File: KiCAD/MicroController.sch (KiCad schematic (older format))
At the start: 0 parts

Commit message: completed 5V buck schematic and setup
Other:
- note added: "atmega and supp"
- note added: "icsp and reset"
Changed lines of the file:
@@
 LIBS:contrib
 LIBS:valves
+LIBS:TPS565208
 LIBS:OBC-PDB-cache
 EELAYER 25 0
@@
 $Descr A4 11693 8268
 encoding utf-8
-Sheet 1 6
+Sheet 3 6
 Title ""
 Date ""
@@
 Comment4 ""
 $EndDescr
+Text Notes 3650 2250 0    118  ~ 0
+atmega and supp
+Text Notes 8400 1950 0    118  ~ 0
+icsp and reset
 $EndSCHEMATC

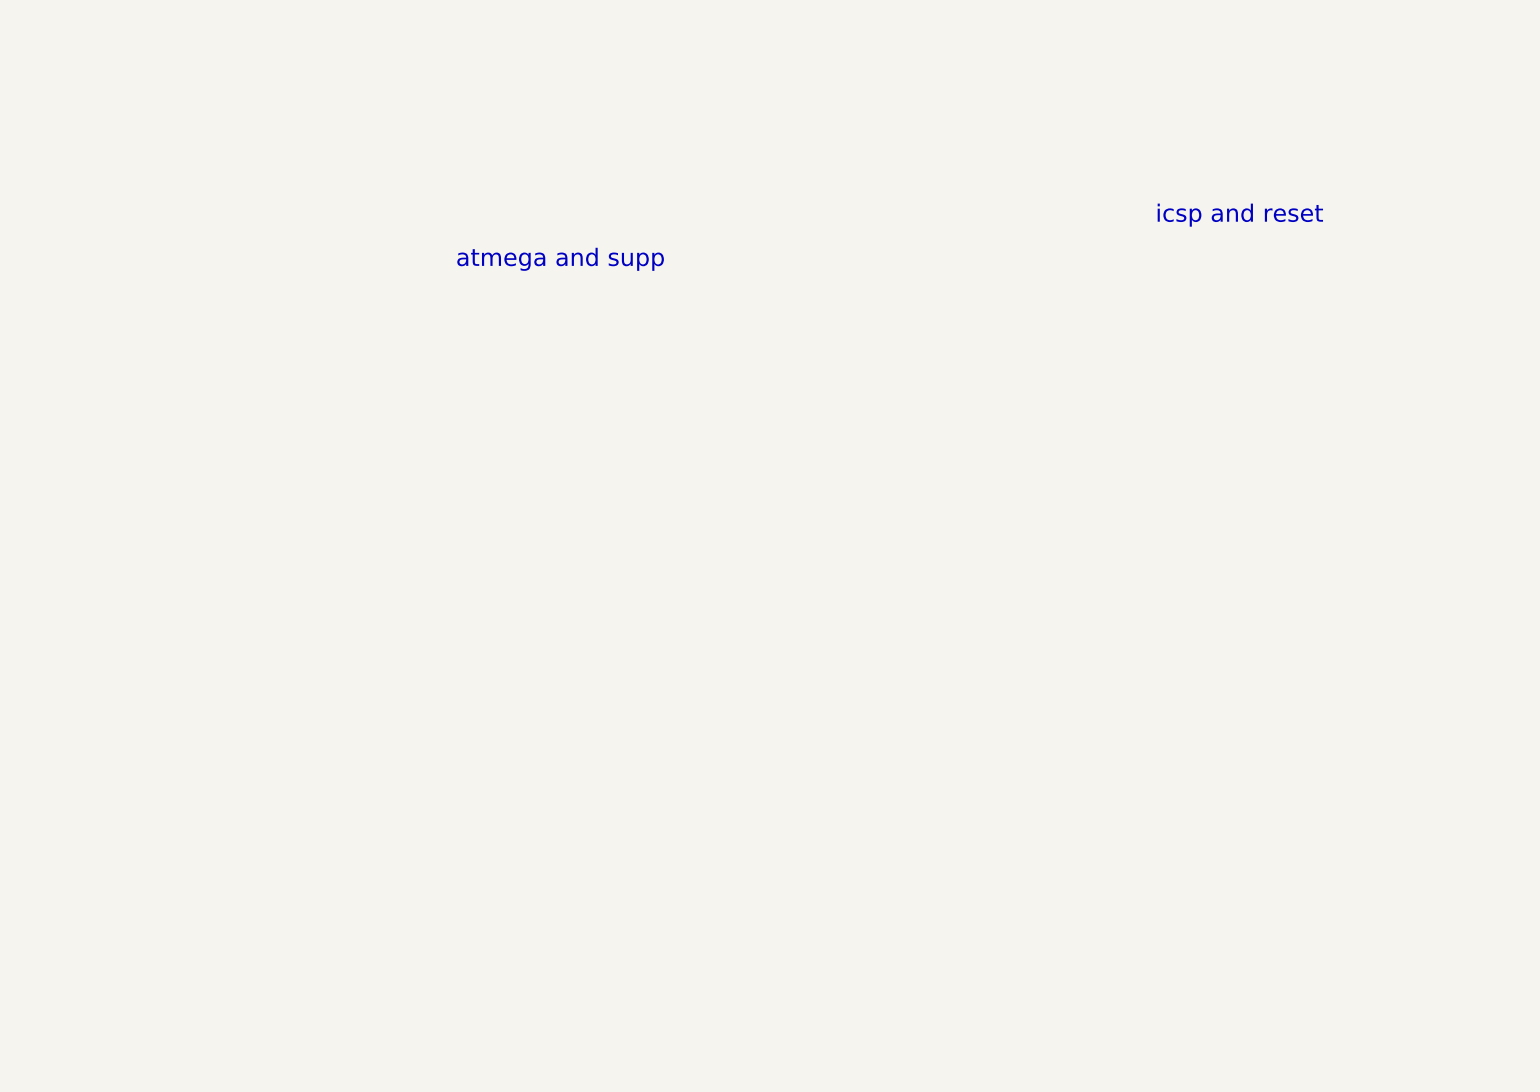
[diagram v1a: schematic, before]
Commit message: added MC but N/C
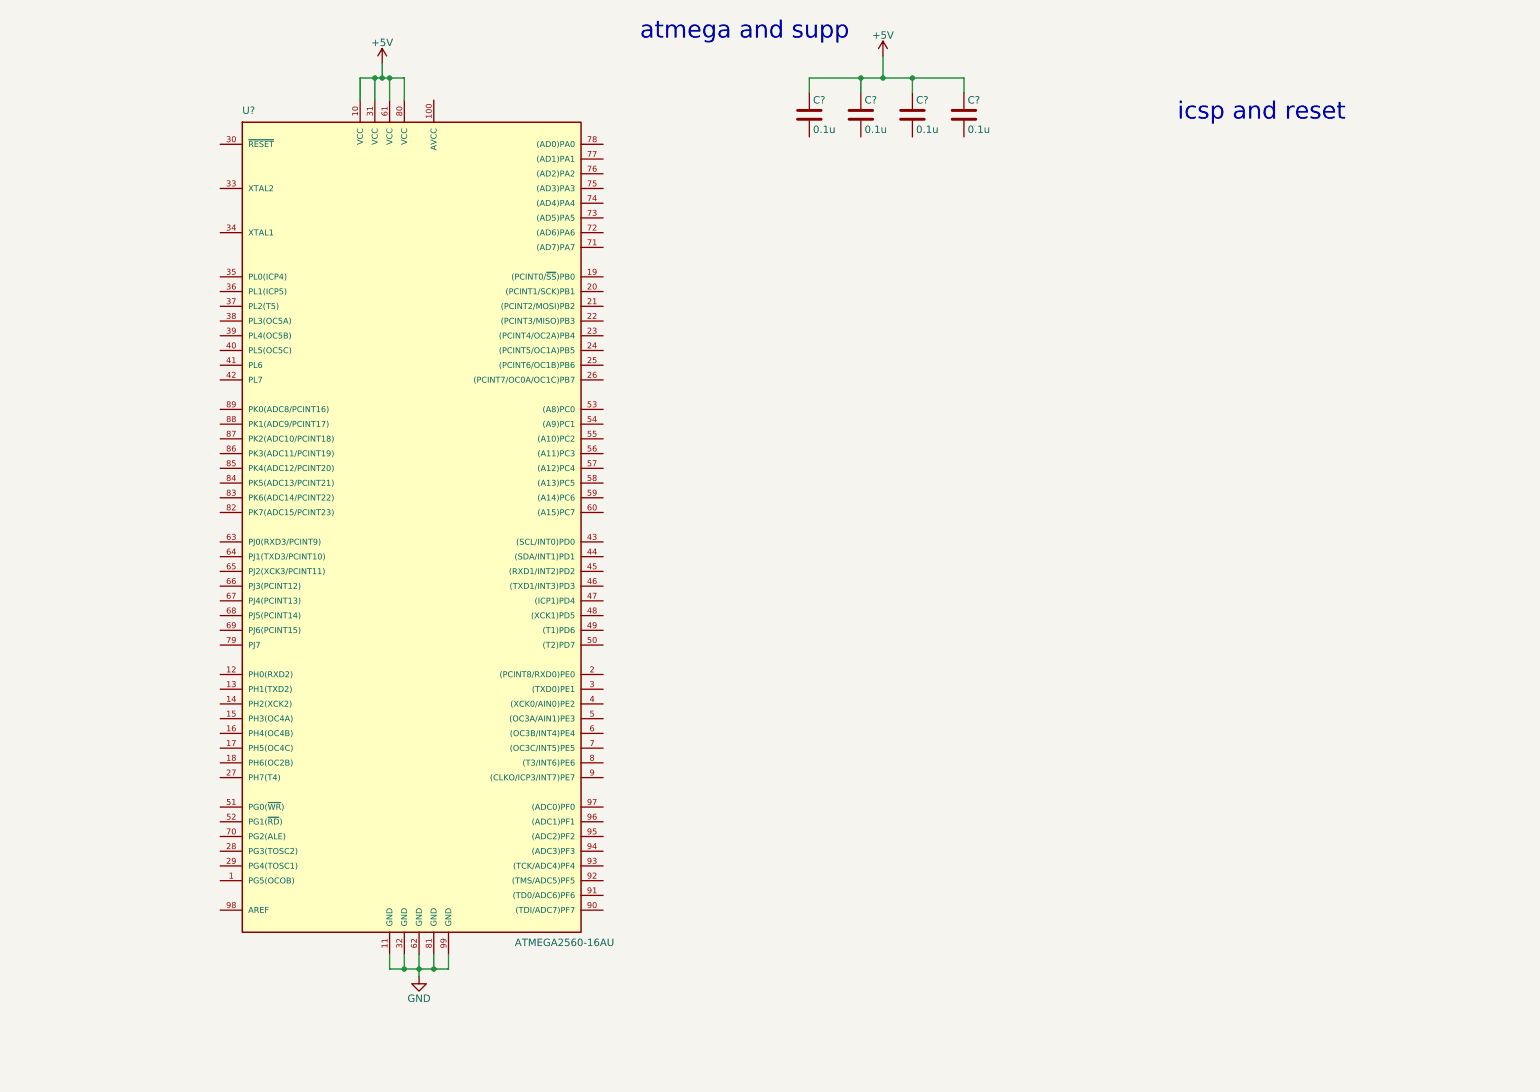
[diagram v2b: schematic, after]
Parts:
- added C? (x4): 0.1u, Capacitors_SMD:C_0805, symbol C
- added U?: ATMEGA2560-16AU, TQFP100, symbol ATMEGA2560-16AU
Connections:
- new net +5V: C?.1, C?.1, C?.1, C?.1, U?.10 (VCC), U?.31 (VCC), U?.61 (VCC), U?.80 (VCC)
- new net GND: U?.11 (GND), U?.32 (GND), U?.62 (GND), U?.81 (GND), U?.99 (GND)
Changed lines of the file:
@@
 Comment4 ""
 $EndDescr
-Text Notes 3650 2250 0    118  ~ 0
+Text Notes 4900 700  0    118  ~ 0
 atmega and supp
-Text Notes 8400 1950 0    118  ~ 0
+Text Notes 8550 1250 0    118  ~ 0
 icsp and reset
+$Comp
+L ATMEGA2560-16AU U?
+U 1 1 5A91BCEE
+P 3350 4000
+F 0 "U?" H 2200 6800 50  0000 L BNN
+F 1 "ATMEGA2560-16AU" H 4050 1150 50  0000 L BNN
+F 2 "TQFP100" H 3350 4000 50  0001 C CIN
+F 3 "http://ww1.microchip.com/downloads/en/DeviceDoc/Atmel-2549-8-bit-AVR-Microcontroller-ATmega640-1280-1281-2560-2561_datasheet.pdf" H 3350 4000 50  0001 C CNN
+	1    3350 4000
+	1    0    0    -1
+$EndComp
+$Comp
+L GND #PWR?
+U 1 1 5A91BF4A
+P 3400 7050
+F 0 "#PWR?" H 3400 6800 50  0001 C CNN
+F 1 "GND" H 3400 6900 50  0000 C CNN
+F 2 "" H 3400 7050 50  0001 C CNN
+F 3 "" H 3400 7050 50  0001 C CNN
+	1    3400 7050
+	1    0    0    -1
+$EndComp
+Wire Wire Line
+	3200 6900 3200 7000
+Wire Wire Line
+	3200 7000 3600 7000
+Wire Wire Line
+	3400 6900 3400 7050
+Wire Wire Line
+	3600 7000 3600 6900
+Connection ~ 3400 7000
+Wire Wire Line
+	3500 6900 3500 7000
+Connection ~ 3500 7000
+Wire Wire Line
+	3300 6900 3300 7000
+Connection ~ 3300 7000
+$Comp
+L +5V #PWR?
+U 1 1 5A91C010
+P 3150 850
+F 0 "#PWR?" H 3150 700 50  0001 C CNN
+F 1 "+5V" H 3150 990 50  0000 C CNN
+F 2 "" H 3150 850 50  0001 C CNN
+F 3 "" H 3150 850 50  0001 C CNN
+	1    3150 850
+	1    0    0    -1
+$EndComp
+Wire Wire Line
+	3000 1100 3000 950
+Wire Wire Line
+	3000 950  3300 950
+Wire Wire Line
+	3150 950  3150 850
+Wire Wire Line
+	3300 950  3300 1100
+Connection ~ 3150 950
+Wire Wire Line
+	3100 1100 3100 950
+Connection ~ 3100 950
+Wire Wire Line
+	3200 1100 3200 950
+Connection ~ 3200 950
+$Comp
+L C C?
+U 1 1 5A91C090
+P 6050 1200
+F 0 "C?" H 6075 1300 50  0000 L CNN
+F 1 "0.1u" H 6075 1100 50  0000 L CNN
+F 2 "Capacitors_SMD:C_0805" H 6088 1050 50  0001 C CNN
+F 3 "" H 6050 1200 50  0001 C CNN
+	1    6050 1200
+	1    0    0    -1
+$EndComp
+$Comp
+L C C?
+U 1 1 5A91C0D2
+P 6400 1200
+F 0 "C?" H 6425 1300 50  0000 L CNN
+F 1 "0.1u" H 6425 1100 50  0000 L CNN
+F 2 "Capacitors_SMD:C_0805" H 6438 1050 50  0001 C CNN
+F 3 "" H 6400 1200 50  0001 C CNN
+	1    6400 1200
+	1    0    0    -1
+$EndComp
+$Comp
+L C C?
+U 1 1 5A91C0F0
+P 6750 1200
+F 0 "C?" H 6775 1300 50  0000 L CNN
+F 1 "0.1u" H 6775 1100 50  0000 L CNN
+F 2 "Capacitors_SMD:C_0805" H 6788 1050 50  0001 C CNN
+F 3 "" H 6750 1200 50  0001 C CNN
+	1    6750 1200
+	1    0    0    -1
+$EndComp
+$Comp
+L C C?
+U 1 1 5A91C10F
+P 7100 1200
+F 0 "C?" H 7125 1300 50  0000 L CNN
+F 1 "0.1u" H 7125 1100 50  0000 L CNN
+F 2 "Capacitors_SMD:C_0805" H 7138 1050 50  0001 C CNN
+F 3 "" H 7100 1200 50  0001 C CNN
+	1    7100 1200
+	1    0    0    -1
+$EndComp
+Wire Wire Line
+	6050 1050 6050 950
+Wire Wire Line
+	6050 950  7100 950
+Wire Wire Line
+	7100 950  7100 1050
+Wire Wire Line
+	6750 1050 6750 950
+Connection ~ 6750 950
+Wire Wire Line
+	6400 1050 6400 950
+Connection ~ 6400 950
+$Comp
+L +5V #PWR?
+U 1 1 5A91C19A
+P 6550 800
+F 0 "#PWR?" H 6550 650 50  0001 C CNN
+F 1 "+5V" H 6550 940 50  0000 C CNN
+F 2 "" H 6550 800 50  0001 C CNN
+F 3 "" H 6550 800 50  0001 C CNN
+	1    6550 800
+	1    0    0    -1
+$EndComp
+Wire Wire Line
+	6550 800  6550 950
+Connection ~ 6550 950
 $EndSCHEMATC

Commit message: µC ATMEGA2560 added and pins labeled, w/ supp components
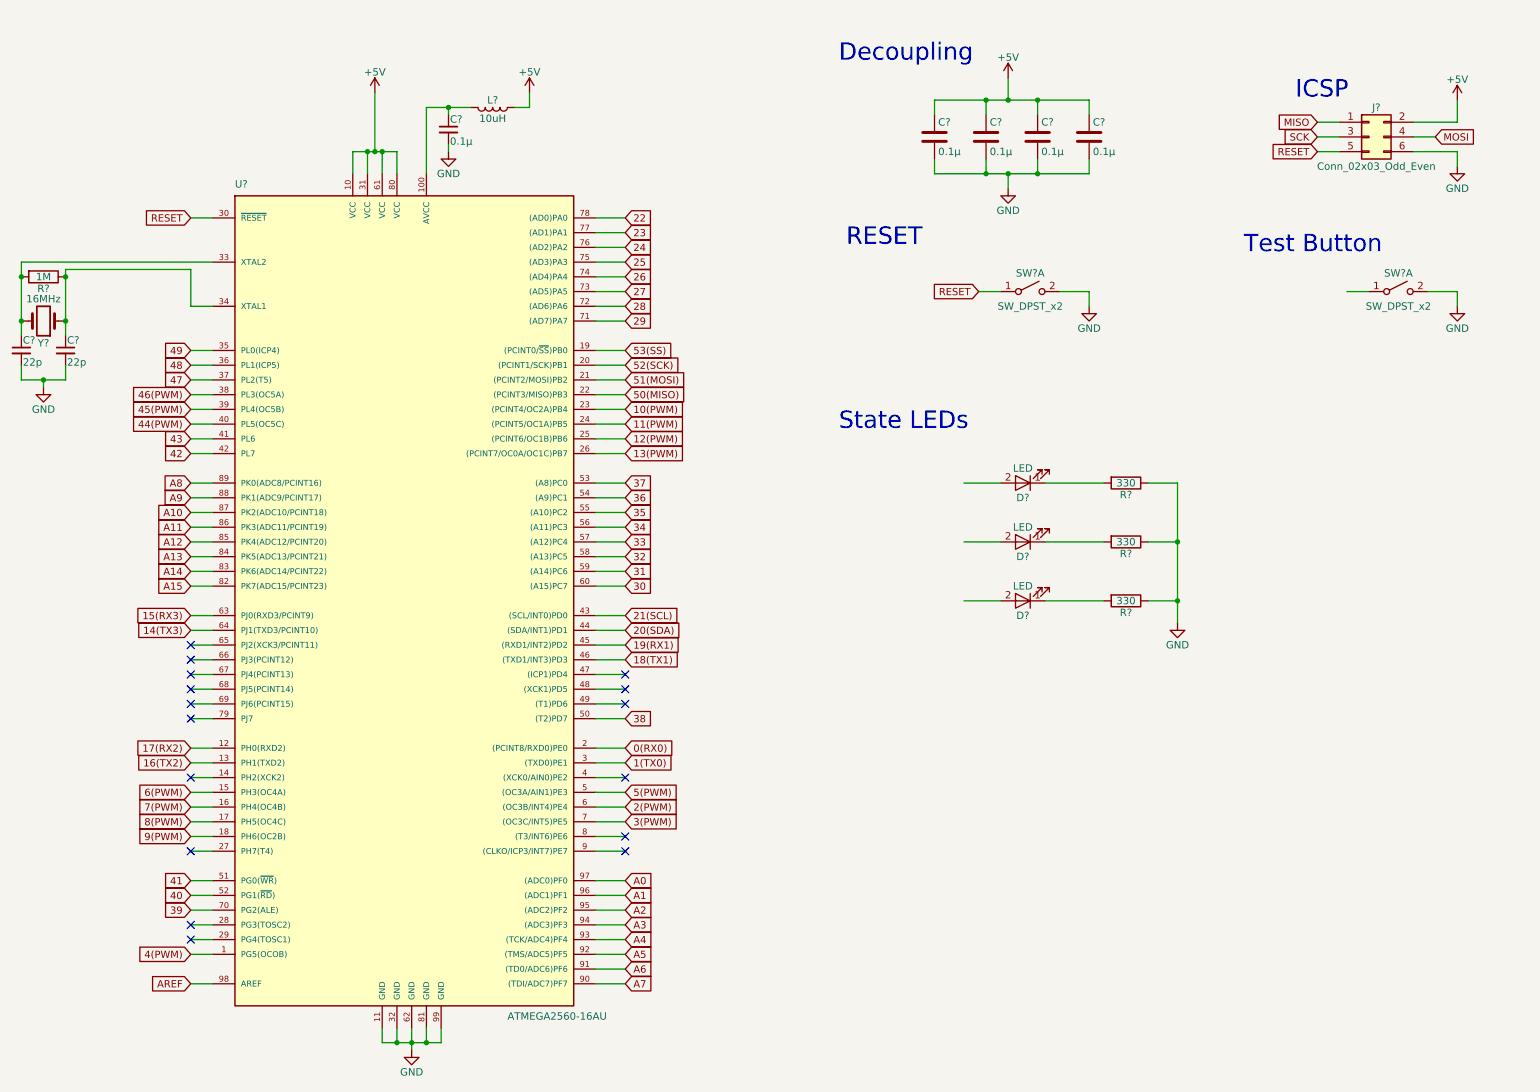
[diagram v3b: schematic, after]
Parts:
- added C? (x2): 22p, Capacitors_SMD:C_0805, symbol C_Small
- added C?: 0.1µ, Capacitors_SMD:C_0805, symbol C_Small
- added D? (x3): LED, symbol LED
- added J?: Conn_02x03_Odd_Even, symbol Conn_02x03_Odd_Even
- added L?: 10uH, symbol L
- added R?: 1M, Resistors_SMD:R_0805, symbol R
- added R? (x3): 330, Resistors_SMD:R_0805, symbol R
- added SW? (x2): SW_DPST_x2, symbol SW_DPST_x2
- added Y?: 16MHz, symbol Crystal
- C? (x4): value 0.1u -> 0.1µ
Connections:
- net +5V: now also J?.2 (Pin_2), L?.1
- net GND: now also C?.2, C?.2, C?.2, C?.2, C?.2, C?.2, C?.2, J?.6 (Pin_6), R?.1, R?.1, R?.1, SW?.2 (B), SW?.2 (B)
- net 4(PWM): now reaches U?.1 (PG5(OCOB))
- net at U?.100 (AVCC): now also C?.1, L?.2
- net 17(RX2): now reaches U?.12 (PH0(RXD2))
- net 16(TX2): now reaches U?.13 (PH1(TXD2))
- net 6(PWM): now reaches U?.15 (PH3(OC4A))
- net 7(PWM): now reaches U?.16 (PH4(OC4B))
- net 8(PWM): now reaches U?.17 (PH5(OC4C))
- net 9(PWM): now reaches U?.18 (PH6(OC2B))
- net 53(SS): now reaches U?.19 ((PCINT0/~SS~)PB0)
- net 0(RX0): now reaches U?.2 ((PCINT8/RXD0)PE0)
- net 52(SCK): now reaches U?.20 ((PCINT1/SCK)PB1)
- net 51(MOSI): now reaches U?.21 ((PCINT2/MOSI)PB2)
- net 50(MISO): now reaches U?.22 ((PCINT3/MISO)PB3)
- net 10(PWM): now reaches U?.23 ((PCINT4/OC2A)PB4)
- net 11(PWM): now reaches U?.24 ((PCINT5/OC1A)PB5)
- net 12(PWM): now reaches U?.25 ((PCINT6/OC1B)PB6)
- net 13(PWM): now reaches U?.26 ((PCINT7/OC0A/OC1C)PB7)
- net 1(TX0): now reaches U?.3 ((TXD0)PE1)
- net RESET: now reaches U?.30 (~RESET)
- net RESET: now also J?.5 (Pin_5), SW?.1 (A)
- net at U?.33 (XTAL2): now also C?.1, R?.2, Y?.2
- net at U?.34 (XTAL1): now also C?.1, R?.1, Y?.1
- net 49: now reaches U?.35 (PL0(ICP4))
- net 48: now reaches U?.36 (PL1(ICP5))
- net 47: now reaches U?.37 (PL2(T5))
- net 46(PWM): now reaches U?.38 (PL3(OC5A))
- net 45(PWM): now reaches U?.39 (PL4(OC5B))
- net 44(PWM): now reaches U?.40 (PL5(OC5C))
- net 43: now reaches U?.41 (PL6)
- net 42: now reaches U?.42 (PL7)
- net 21(SCL): now reaches U?.43 ((SCL/INT0)PD0)
- net 20(SDA): now reaches U?.44 ((SDA/INT1)PD1)
- net 19(RX1): now reaches U?.45 ((RXD1/INT2)PD2)
- net 18(TX1): now reaches U?.46 ((TXD1/INT3)PD3)
- net 5(PWM): now reaches U?.5 ((OC3A/AIN1)PE3)
- net 38: now reaches U?.50 ((T2)PD7)
- net 41: now reaches U?.51 (PG0(~WR~))
- net 40: now reaches U?.52 (PG1(~RD~))
- net 37: now reaches U?.53 ((A8)PC0)
- net 36: now reaches U?.54 ((A9)PC1)
- net 35: now reaches U?.55 ((A10)PC2)
- net 34: now reaches U?.56 ((A11)PC3)
- net 33: now reaches U?.57 ((A12)PC4)
- net 32: now reaches U?.58 ((A13)PC5)
- net 31: now reaches U?.59 ((A14)PC6)
- net 2(PWM): now reaches U?.6 ((OC3B/INT4)PE4)
- net 30: now reaches U?.60 ((A15)PC7)
- net 15(RX3): now reaches U?.63 (PJ0(RXD3/PCINT9))
- net 14(TX3): now reaches U?.64 (PJ1(TXD3/PCINT10))
- net 3(PWM): now reaches U?.7 ((OC3C/INT5)PE5)
- net 39: now reaches U?.70 (PG2(ALE))
- net 29: now reaches U?.71 ((AD7)PA7)
- net 28: now reaches U?.72 ((AD6)PA6)
- net 27: now reaches U?.73 ((AD5)PA5)
- net 26: now reaches U?.74 ((AD4)PA4)
- net 25: now reaches U?.75 ((AD3)PA3)
- net 24: now reaches U?.76 ((AD2)PA2)
- net 23: now reaches U?.77 ((AD1)PA1)
- net 22: now reaches U?.78 ((AD0)PA0)
- net A15: now reaches U?.82 (PK7(ADC15/PCINT23))
- net A14: now reaches U?.83 (PK6(ADC14/PCINT22))
- net A13: now reaches U?.84 (PK5(ADC13/PCINT21))
- net A12: now reaches U?.85 (PK4(ADC12/PCINT20))
- net A11: now reaches U?.86 (PK3(ADC11/PCINT19))
- net A10: now reaches U?.87 (PK2(ADC10/PCINT18))
- net A9: now reaches U?.88 (PK1(ADC9/PCINT17))
- net A8: now reaches U?.89 (PK0(ADC8/PCINT16))
- net A7: now reaches U?.90 ((TDI/ADC7)PF7)
- net A6: now reaches U?.91 ((TD0/ADC6)PF6)
- net A5: now reaches U?.92 ((TMS/ADC5)PF5)
- net A4: now reaches U?.93 ((TCK/ADC4)PF4)
- net A3: now reaches U?.94 ((ADC3)PF3)
- net A2: now reaches U?.95 ((ADC2)PF2)
- net A1: now reaches U?.96 ((ADC1)PF1)
- net A0: now reaches U?.97 ((ADC0)PF0)
- net AREF: now reaches U?.98 (AREF)
- new net: D?.1 (K), R?.2 (x3)
- new net MISO: J?.1 (Pin_1)
- new net MOSI: J?.4 (Pin_4)
- new net SCK: J?.3 (Pin_3)
- no-connect marks 0 -> 16
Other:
- note added: "Decoupling\n"
- note added: "ICSP"
- note added: "RESET"
- note added: "State LEDs"
- note added: "Test Button"
- note removed: "atmega and supp"
- note removed: "icsp and reset"
- moved on the sheet: C?, U?

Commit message: Schematic small fix
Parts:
- added MK1: Mounting_Hole, Mounting_Holes:MountingHole_3.2mm_M3, symbol Mounting_Hole
- added MK2, MK3, MK4: Mounting_Hole, symbol Mounting_Hole
- D4: renamed from D?; value LED -> 110; footprint (none) -> LEDs:LED_0805
- D5, D6: renamed from D?; footprint (none) -> LEDs:LED_0805
- J2: renamed from J?; footprint (none) -> Pin_Headers:Pin_Header_Straight_2x03_Pitch2.54mm
- R7, R8, R9: renamed from R?; value 330 -> 110
- SW1: renamed from SW?; footprint (none) -> Buttons_Switches_SMD:SW_SPST_B3U-1000P
- U3: renamed from U?; footprint TQFP100 -> Housings_QFP:TQFP-100_14x14mm_Pitch0.5mm
- gave numbers to parts that had none: 10
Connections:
- net GND: now also SW1.4 (B); no longer SW1.2 (B)
